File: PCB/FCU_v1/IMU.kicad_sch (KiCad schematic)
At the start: 26 parts, among them IC1 BMM350, IC2 TPS7A2018PDBVR, U2 BMP581, U4 BMI088

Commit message: Repaired library
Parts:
- removed IC1: BMM350, BGA9C40P3X3_128X128X54, symbol SamacSys_Parts:BMM350
- removed IC2: TPS7A2018PDBVR, SOT95P280X145-5N, symbol SamacSys_Parts:TPS7A2018PDBVR
- removed U2: BMP581, BMP581, symbol SamacSys_Parts:BMP581
- added IC2: BMM350, BGA9C40P3X3_128X128X54, symbol SamacSys_Parts:BMM350
- added IC3: TPS7A2018PDBVR, SOT95P280X145-5N, symbol SamacSys_Parts:TPS7A2018PDBVR
- added U7: BMP581, BMP581, symbol SamacSys_Parts:BMP581
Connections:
- net +3.3V: now also IC2.B3 (VDDIO), IC3.1 (IN), IC3.3 (EN), U7.1 (VDDIO), U7.10 (VDD), U7.6 (CSB)
- net BAR_INT: now also U7.7 (INT)
- net GND: now also IC2.B1 (GND), IC2.C3 (BYPASS), IC3.2 (GND), U7.3 (VSS), U7.8 (VSS), U7.9 (VSS)
- net I2C_SCK: now also IC2.A3 (SCK), U7.2 (SCK)
- net I2C_SDA: now also IC2.A2 (SDA), U7.4 (SDI)
- net MAG_INT: now also IC2.A1 (INT)
- net at C18.1, C36.1: now also IC2.C1 (VDD), IC3.5 (OUT)
- net at R41.2, R42.1: now also U7.5 (SDO)
- net at C3.1: now also IC2.C2 (CRST)
- net at R38.1, R39.2: now also IC2.B2 (ADSEL)

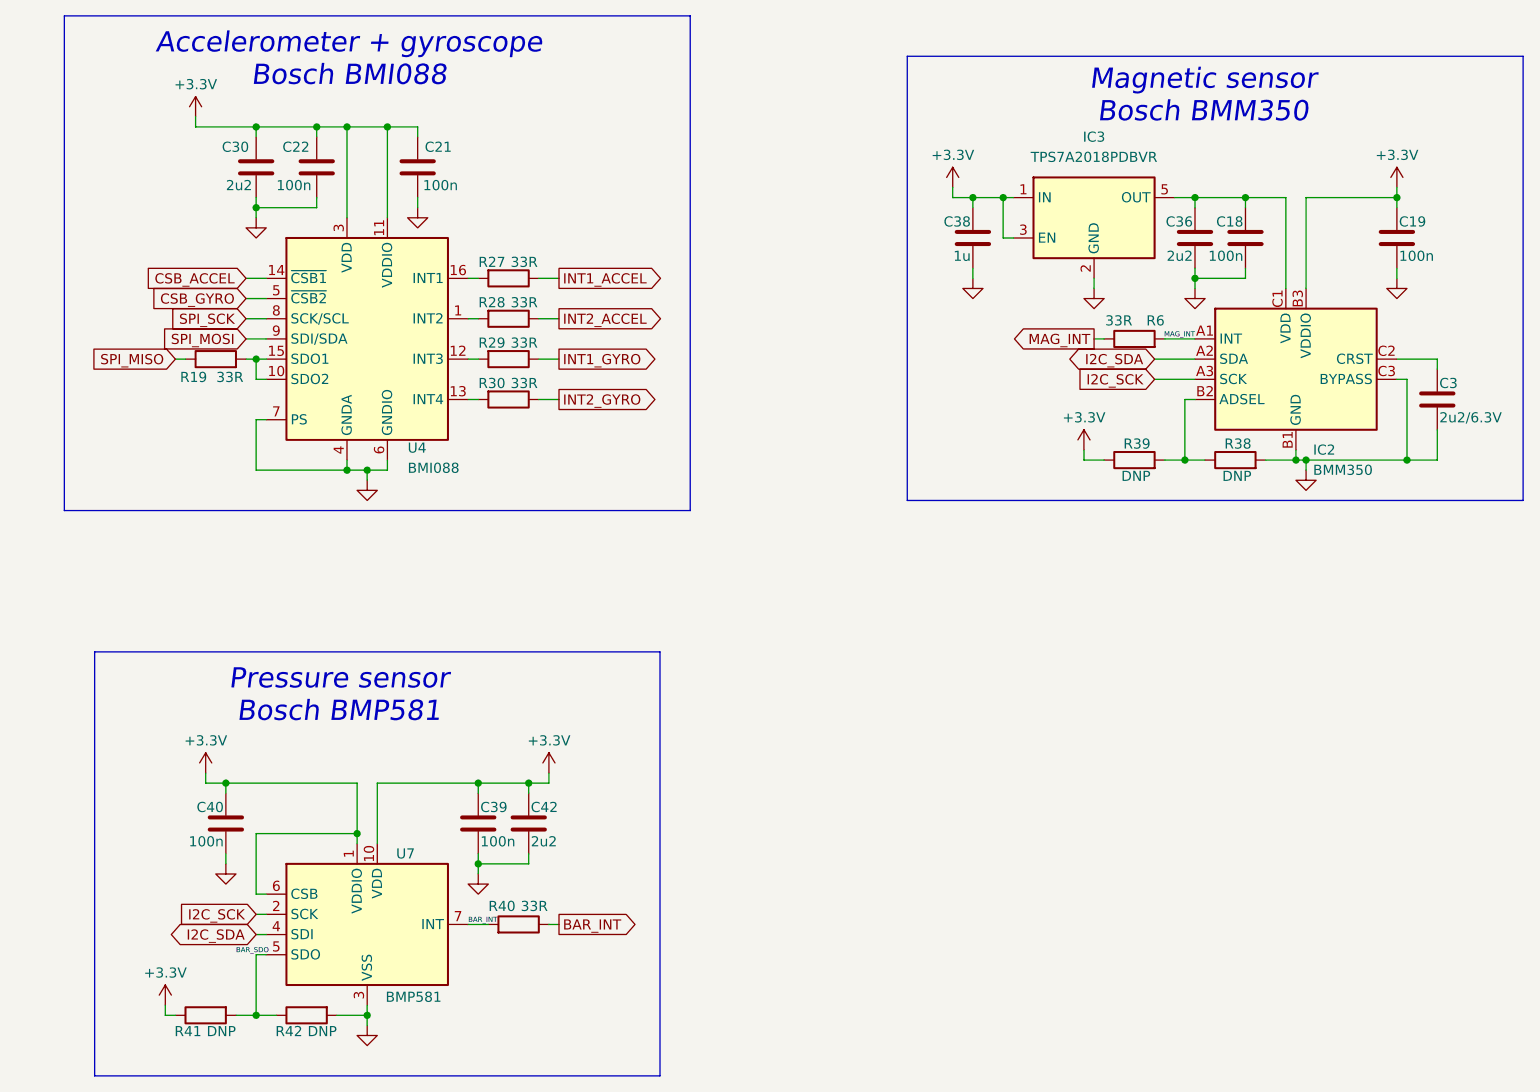
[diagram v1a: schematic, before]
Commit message: Components change and layout update
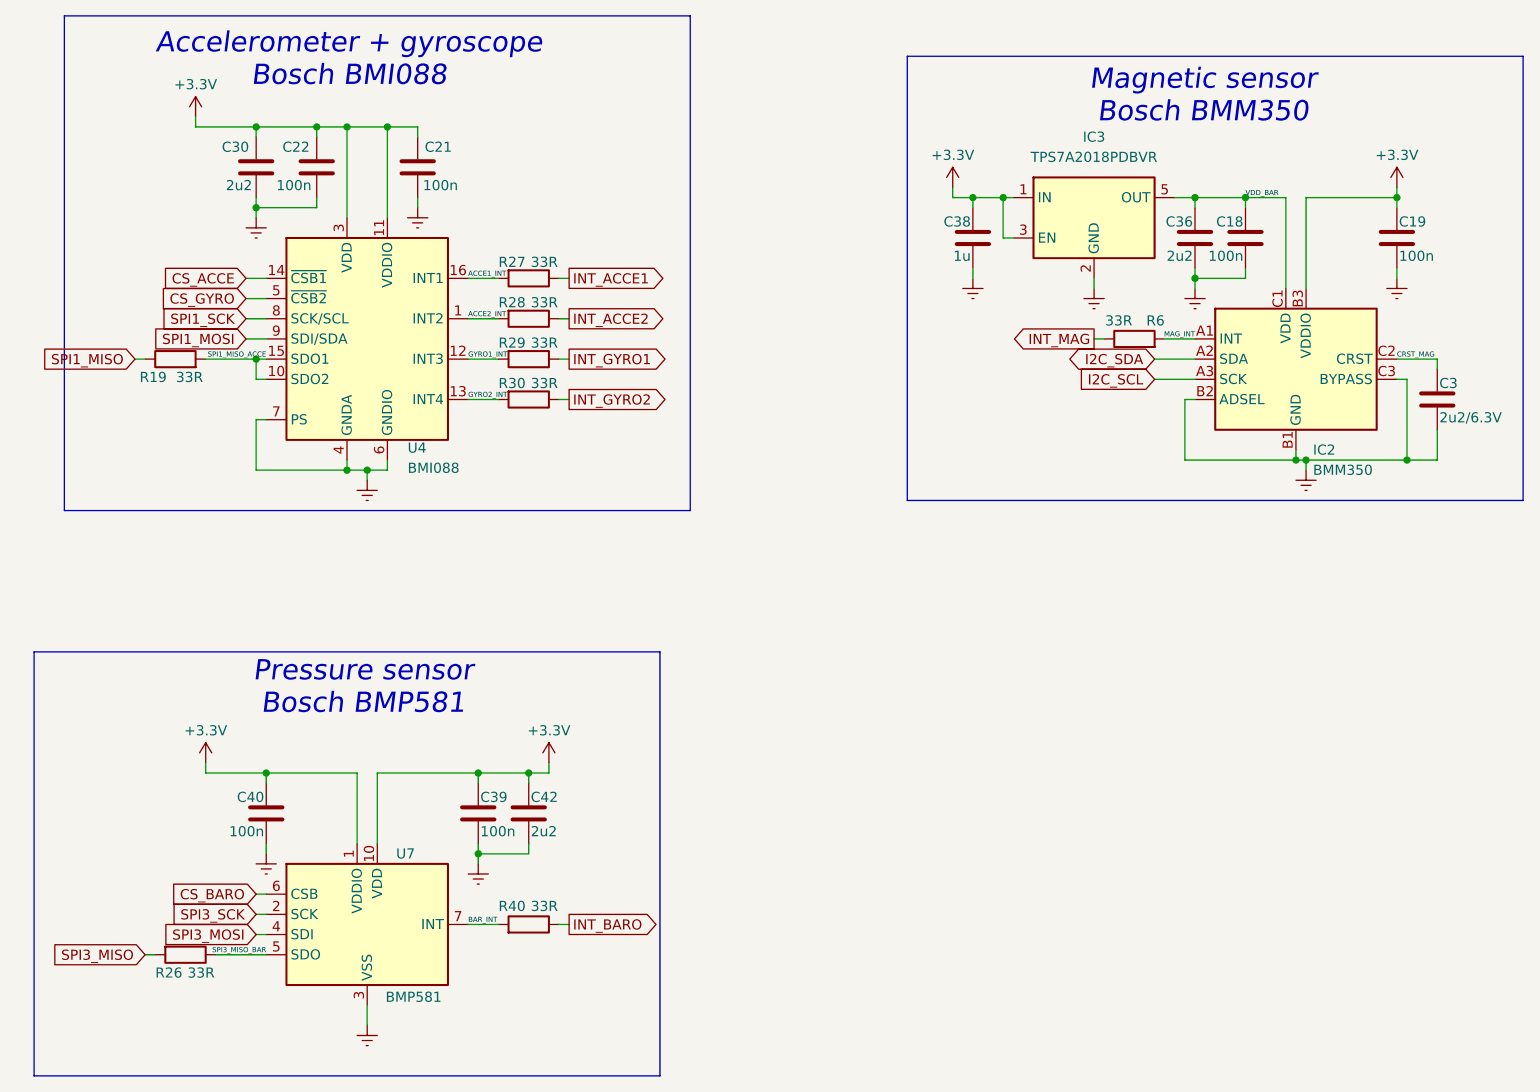
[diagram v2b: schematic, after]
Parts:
- removed R38, R39, R41, R42: DNP, Resistor_SMD:R_0201_0603Metric, symbol Device:R
- added R26: 33R, Resistor_SMD:R_0603_1608Metric, symbol Device:R
- C22, C39, C40: footprint Capacitor_SMD:C_0805_2012Metric -> Capacitor_SMD:C_0603_1608Metric
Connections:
- net +3.3V: no longer U7.6 (CSB)
- net BAR_INT: no longer R40.1
- net GND: now also IC2.B2 (ADSEL)
- net I2C_SDA: no longer U7.4 (SDI)
- net MAG_INT: no longer R6.1
- net VDD_BAR: now reaches C18.1, C36.1, IC2.C1 (VDD), IC3.5 (OUT)
- net SPI3_MISO_BAR: now reaches U7.5 (SDO)
- net SPI3_MISO_BAR: now also R26.1
- net CRST_MAG: now reaches C3.1, IC2.C2 (CRST)
- net ACCE2_INT: now reaches R28.2, U4.1 (INT2)
- net GYRO2_INT: now reaches R30.2, U4.13 (INT4)
- net SPI1_MISO_ACCE: now reaches R19.2, U4.10 (SDO2), U4.15 (SDO1)
- net ACCE1_INT: now reaches R27.2, U4.16 (INT1)
- net GYRO1_INT: now reaches R29.2, U4.12 (INT3)
- net CSB_ACCEL renamed CS_ACCE
- net CSB_GYRO renamed CS_GYRO
- net I2C_SCK renamed I2C_SCL
- net I2C_SCL: no longer U7.2 (SCK)
- net INT1_ACCEL renamed INT_ACCE1
- net INT1_GYRO renamed INT_GYRO1
- net INT2_ACCEL renamed INT_ACCE2
- net INT2_GYRO renamed INT_GYRO2
- net SPI_MISO renamed SPI1_MISO
- net SPI_MOSI renamed SPI1_MOSI
- net SPI_SCK renamed SPI1_SCK
- new net CS_BARO: U7.6 (CSB)
- new net INT_BARO: R40.1
- new net INT_MAG: R6.1
- new net SPI3_MISO: R26.2
- new net SPI3_MOSI: U7.4 (SDI)
- new net SPI3_SCK: U7.2 (SCK)
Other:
- moved on the sheet: C39, C40, C42, R19, R27, R28, R29, R30, R40

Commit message: Layout update
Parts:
- removed IC2: BMM350, BGA9C40P3X3_128X128X54, symbol SamacSys_Parts:BMM350
- removed IC3: TPS7A2018PDBVR, SOT95P280X145-5N, symbol SamacSys_Parts:TPS7A2018PDBVR
- removed U7: BMP581, BMP581, symbol SamacSys_Parts:BMP581
- added IC1: BMM350, BGA9C40P3X3_128X128X54, symbol SamacSys_Parts:BMM350
- added IC4: TPS7A2018PDBVR, SOT95P280X145-5N, symbol SamacSys_Parts:TPS7A2018PDBVR
- added U8: BMP581, BMP581, symbol SamacSys_Parts:BMP581
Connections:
- net +3.3V: now also IC1.B3 (VDDIO), IC4.1 (IN), IC4.3 (EN), U8.1 (VDDIO), U8.10 (VDD)
- net BAR_INT: now also U8.7 (INT)
- net CRST_MAG: now also IC1.C2 (CRST)
- net CS_BARO: now also U8.6 (CSB)
- net GND: now also IC1.B1 (GND), IC1.B2 (ADSEL), IC1.C3 (BYPASS), IC4.2 (GND), U8.3 (VSS), U8.8 (VSS), U8.9 (VSS)
- net I2C_SCL: now also IC1.A3 (SCK)
- net I2C_SDA: now also IC1.A2 (SDA)
- net MAG_INT: now also IC1.A1 (INT)
- net SPI3_MISO_BAR: now also U8.5 (SDO)
- net SPI3_MOSI: now also U8.4 (SDI)
- net SPI3_SCK: now also U8.2 (SCK)
- net VDD_BAR: now also IC1.C1 (VDD), IC4.5 (OUT)
